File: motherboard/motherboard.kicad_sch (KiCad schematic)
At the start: 57 parts, among them U1 QT1481, U2 cap_touch, U3 cap_touch, k1 cap_touch, k10 cap_touch, k11 cap_touch, k12 cap_touch, k13 cap_touch, k14 cap_touch, k15 cap_touch, k2 cap_touch, k3 cap_touch, k4 cap_touch, k5 cap_touch, k6 cap_touch, k7 cap_touch, k8 cap_touch, k9 cap_touch

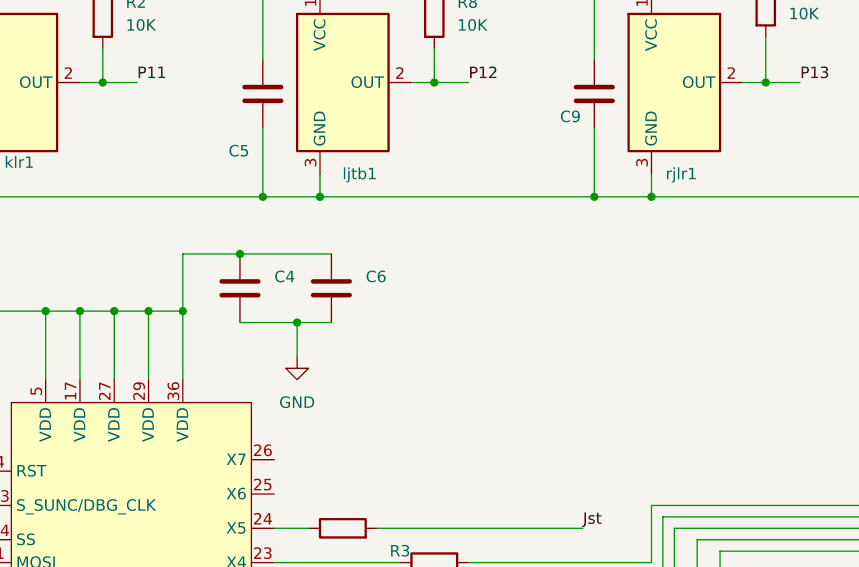
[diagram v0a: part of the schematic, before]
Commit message: fix error hall
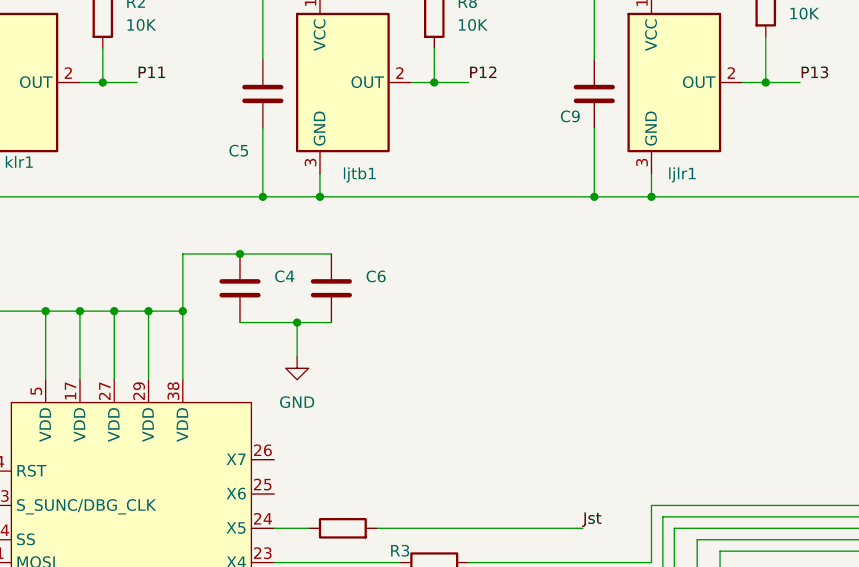
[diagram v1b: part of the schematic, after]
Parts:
- renumbered rjlr1 to ljlr1
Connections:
- net +5V: now also U1.38 (VDD); no longer U1.36 (Y5A)
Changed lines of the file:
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@@
     (pin "34")
     (pin "35")
-    (pin "36")
+    (pin "38")
     (pin "36")
     (pin "37")
@@
   (symbol (lib_id "Sensor_Magnetic:DRV5055A1xDBZxQ1") (at 180.34 44.45 0) (unit 1)
     (in_bom yes) (on_board yes)
-    (property "Reference" "rjlr1" (id 0) (at 182.88 54.61 0)
+    (property "Reference" "ljlr1" (id 0) (at 182.88 54.61 0)
       (effects (font (size 1.27 1.27)) (justify right))
     )
@@
       (reference "ktb1") (unit 1) (value "DRV505") (footprint "Package_TO_SOT_SMD:SOT-23")
     )
+    (path "/a7594aa7-ff91-417c-8749-70aad5ba1e56"
+      (reference "ljlr1") (unit 1) (value "DRV505") (footprint "Package_TO_SOT_SMD:SOT-23")
+    )
     (path "/11d88314-ce06-44e4-976a-1a9db8567436"
       (reference "ljtb1") (unit 1) (value "DRV505") (footprint "Package_TO_SOT_SMD:SOT-23")
     )
-    (path "/a7594aa7-ff91-417c-8749-70aad5ba1e56"
-      (reference "rjlr1") (unit 1) (value "DRV505") (footprint "Package_TO_SOT_SMD:SOT-23")
-    )
     (path "/6bc6018a-8b24-480a-b8c5-125304420071"

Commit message: 3dmother
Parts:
- removed k1, k10, k11, k12, k13, k14, k15, k2, k3, k4, k5, k6, k7, k8, k9: cap_touch, 42QT1481:cap_touch, symbol touch_keys:cap_touch
- added C23, C24, C25, C26, C27, C28, C29, C30, C31, C32, C33, C34, C35, C36, C37, C38, C39, C40, C41, C42, C43, C44, C45, C46, C47, C48, C49, C50, C51, C52, C53, C54, C55, C56: 50pF, Capacitor_Tantalum_SMD:CP_EIA-1608-10_AVX-L_Pad1.25x1.05mm_HandSolder, symbol Device:C
- added U23, U24, U25, U26, U27, U28, U29, U30, U31, U32, U33, U34, U35, U36, U37: cap_touch, 42QT1481:cap_touch, symbol touch_keys:cap_touch
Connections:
- net y3: now reaches R16.2
- net y3: now also C44.2, C46.2, C48.2, C50.2, C52.2
- net at R10.2: now also C31.1, C41.1, C51.1
- net y1: now reaches R13.2
- net y1: now also C24.2, C26.2, C28.2, C30.2, C32.2
- net at R12.2: now also C29.1, C39.1, C49.1
- net x0: now reaches R5.2
- net x0: now also C54.2, C56.2
- net at R4.2: now also C27.1, C37.1, C47.1
- net y2: now reaches R15.2
- net y2: now also C34.2, C36.2, C38.2, C40.2, C42.2
- net at R9.2: now also C25.1, C35.1, C45.1
- net Jst: no longer names the net of R3.2
- net Jst: now also C23.1, C33.1, C43.1
- net jst: no longer names the net of U2.1 (C1)
- net jst: now also C23.2, C24.1; no longer U3.1 (C1)
- new net: C47.2, C48.1, U33.1 (C1)
- new net: C39.2, C40.1, U29.1 (C1)
- new net: C31.2, C32.1, U25.1 (C1)
- new net: C33.2, C34.1, U26.1 (C1)
- new net: C37.2, C38.1, U28.1 (C1)
- new net: C35.2, C36.1, U27.1 (C1)
- new net: C53.2, C54.1, U36.1 (C1)
- new net: C43.2, C44.1, U31.1 (C1)
- new net: C27.2, C28.1, U23.1 (C1)
- new net: C55.1, R18.2
- new net: C55.2, C56.1, U37.1 (C1)
- new net: C41.2, C42.1, U30.1 (C1)
- new net: C45.2, C46.1, U32.1 (C1)
- new net: C51.2, C52.1, U35.1 (C1)
- new net: C29.2, C30.1, U24.1 (C1)
- new net: C49.2, C50.1, U34.1 (C1)
- new net: C25.2, C26.1, U3.1 (C1)
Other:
- moved on the sheet: C10, C11, C3, C4, C6, C7, C8, R10, R11, R12, R13, R14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

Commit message: cp10 to A0
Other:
- sheet Mouse_and_microcontroller ports: added ADC_0, ADC_1; removed GP10, GP11
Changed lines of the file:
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@@
       (effects (font (size 1.27 1.27)) (justify right))
     )
-    (pin "GP10" input (at 54.61 109.22 0)
+    (pin "ADC_0" input (at 54.61 109.22 0)
       (effects (font (size 1.27 1.27)) (justify right))
     )
-    (pin "GP11" input (at 54.61 113.03 0)
+    (pin "ADC_1" input (at 54.61 113.03 0)
       (effects (font (size 1.27 1.27)) (justify right))
     )

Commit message: oh49e
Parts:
- removed R1, R2: 10K, Resistor_SMD:R_0805_2012Metric_Pad1.20x1.40mm_HandSolder, symbol Device:R
- klr1, ktb1: value DRV505 -> (none)
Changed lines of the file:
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@@
   (junction (at 140.97 57.15) (diameter 0) (color 0 0 0 0)
   )
-  (junction (at 116.84 44.45) (diameter 0) (color 0 0 0 0)
-  )
   (junction (at 222.25 119.38) (diameter 0) (color 0 0 0 0)
   )
@@
   (junction (at 96.52 69.85) (diameter 0) (color 0 0 0 0)
   )
-  (junction (at 81.28 44.45) (diameter 0) (color 0 0 0 0)
-  )
   (junction (at 193.04 106.68) (diameter 0) (color 0 0 0 0)
   )
@@
     (stroke (width 0) (type default))
   )
-  (wire (pts (xy 114.3 44.45) (xy 116.84 44.45))
+  (wire (pts (xy 114.3 44.45) (xy 120.65 44.45))
     (stroke (width 0) (type default))
   )
@@
     (stroke (width 0) (type default))
   )
-  (wire (pts (xy 116.84 40.64) (xy 116.84 44.45))
-    (stroke (width 0) (type default))
-  )
   (wire (pts (xy 147.32 101.6) (xy 147.32 67.31))
     (stroke (width 0) (type default))
@@
     (stroke (width 0) (type default))
   )
-  (wire (pts (xy 116.84 25.4) (xy 116.84 33.02))
-    (stroke (width 0) (type default))
-  )
   (wire (pts (xy 95.25 165.1) (xy 95.25 171.45))
     (stroke (width 0) (type default))
@@
     (stroke (width 0) (type default))
   )
-  (wire (pts (xy 81.28 33.02) (xy 81.28 26.67))
-    (stroke (width 0) (type default))
-  )
   (wire (pts (xy 259.08 95.25) (xy 259.08 96.52))
     (stroke (width 0) (type default))
@@
     (stroke (width 0) (type default))
   )
-  (wire (pts (xy 116.84 44.45) (xy 120.65 44.45))
-    (stroke (width 0) (type default))
-  )
   (wire (pts (xy 226.06 39.37) (xy 226.06 44.45))
     (stroke (width 0) (type default))
@@
     (stroke (width 0) (type default))
   )
-  (wire (pts (xy 81.28 40.64) (xy 81.28 44.45))
-    (stroke (width 0) (type default))
-  )
   (wire (pts (xy 204.47 128.27) (xy 204.47 130.81))
     (stroke (width 0) (type default))
@@
     (stroke (width 0) (type default))
   )
-  (wire (pts (xy 78.74 44.45) (xy 81.28 44.45))
+  (wire (pts (xy 78.74 44.45) (xy 83.82 44.45))
     (stroke (width 0) (type default))
   )
@@
     (stroke (width 0) (type default))
   )
-  (wire (pts (xy 81.28 44.45) (xy 83.82 44.45))
-    (stroke (width 0) (type default))
-  )
   (wire (pts (xy 166.37 109.22) (xy 166.37 64.77))
     (stroke (width 0) (type default))
@@
     (effects (font (size 1.27 1.27)) (justify left bottom))
   )
-  (label "+3.3V" (at 116.84 25.4 0) (fields_autoplaced)
-    (effects (font (size 1.27 1.27)) (justify left bottom))
-  )
   (label "P15" (at 266.7 44.45 0) (fields_autoplaced)
     (effects (font (size 1.27 1.27)) (justify left bottom))
@@
     (effects (font (size 1.27 1.27)) (justify left bottom))
   )
-  (label "+3.3V" (at 81.28 26.67 0) (fields_autoplaced)
-    (effects (font (size 1.27 1.27)) (justify left bottom))
-  )
   (label "P10" (at 83.82 44.45 0) (fields_autoplaced)
     (effects (font (size 1.27 1.27)) (justify left bottom))
@@
       (effects (font (size 1.27 1.27)) (justify right))
     )
-    (property "Value" "DRV505" (at 100.33 45.7199 0)
+    (property "Value" "" (at 100.33 45.7199 0)
       (effects (font (size 1.27 1.27)) (justify right) hide)
     )
@@
       (effects (font (size 1.27 1.27)) hide)
     )
-    (property "Datasheet" "https://www.ti.com/lit/ds/symlink/drv5055-q1.pdf" (at 106.68 44.45 0)
+    (property "Datasheet" "https://www.progrexa.com/file_PDF/OH49E.pdf" (at 106.68 44.45 0)
       (effects (font (size 1.27 1.27)) hide)
     )
@@
       (effects (font (size 1.27 1.27)) (justify right))
     )
-    (property "Value" "DRV505" (at 64.77 45.7199 0)
+    (property "Value" "" (at 64.77 45.7199 0)
       (effects (font (size 1.27 1.27)) (justify right) hide)
     )
@@
       (effects (font (size 1.27 1.27)) hide)
     )
-    (property "Datasheet" "https://www.ti.com/lit/ds/symlink/drv5055-q1.pdf" (at 71.12 44.45 0)
+    (property "Datasheet" "https://www.progrexa.com/file_PDF/OH49E.pdf" (at 71.12 44.45 0)
       (effects (font (size 1.27 1.27)) hide)
     )
@@
     )
   )
-  (symbol (lib_id "Device:R") (at 116.84 36.83 0) (unit 1)
-    (in_bom yes) (on_board yes) (dnp no) (fields_autoplaced)
-    (property "Reference" "R2" (at 119.38 35.5599 0)
-      (effects (font (size 1.27 1.27)) (justify left))
-    )
-    (property "Value" "10K" (at 119.38 38.0999 0)
-      (effects (font (size 1.27 1.27)) (justify left))
-    )
-    (property "Footprint" "Resistor_SMD:R_0805_2012Metric_Pad1.20x1.40mm_HandSolder" (at 115.062 36.83 90)
-      (effects (font (size 1.27 1.27)) hide)
-    )
-    (property "Datasheet" "~" (at 116.84 36.83 0)
-      (effects (font (size 1.27 1.27)) hide)
-    )
-    (pin "1")
-    (pin "2")
-    (instances
-      (project "motherboard"
-        (path "/99157713-5a67-456e-be9f-48b28b564fb7"
-          (reference "R2") (unit 1)
-        )
-      )
-    )
-  )
   (symbol (lib_id "touch_keys:cap_touch") (at 204.47 85.09 0) (unit 1)
     (in_bom yes) (on_board yes) (dnp no)
@@
         )
       )
-    )
-  )
-  (symbol (lib_id "Device:R") (at 81.28 36.83 0) (unit 1)
-    (in_bom yes) (on_board yes) (dnp no) (fields_autoplaced)
-    (property "Reference" "R1" (at 83.82 35.5599 0)
-      (effects (font (size 1.27 1.27)) (justify left))
-    )
-    (property "Value" "10K" (at 83.82 38.0999 0)
-      (effects (font (size 1.27 1.27)) (justify left))
-    )
-    (property "Footprint" "Resistor_SMD:R_0805_2012Metric_Pad1.20x1.40mm_HandSolder" (at 79.502 36.83 90)
-      (effects (font (size 1.27 1.27)) hide)
-    )
-    (property "Datasheet" "~" (at 81.28 36.83 0)
-      (effects (font (size 1.27 1.27)) hide)
-    )
-    (pin "1")
-    (pin "2")
-    (instances
-      (project "motherboard"
-        (path "/99157713-5a67-456e-be9f-48b28b564fb7"
-          (reference "R1") (unit 1)
-        )
-      )

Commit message: mpr121
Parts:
- removed C10, C11, C7, C8: 4.7nF, Capacitor_Tantalum_SMD:CP_EIA-2012-15_AVX-P_Pad1.30x1.05mm_HandSolder, symbol Device:C
- removed C3: 4.7uF, Capacitor_Tantalum_SMD:CP_EIA-6032-15_Kemet-U_Pad2.25x2.35mm_HandSolder, symbol Device:C
- removed C4, C6: 0.1uF, Capacitor_Tantalum_SMD:CP_EIA-3528-12_Kemet-T_Pad1.50x2.35mm_HandSolder, symbol Device:C
- removed C53, C55: 50pF, Capacitor_Tantalum_SMD:CP_EIA-1608-10_AVX-L_Pad1.25x1.05mm_HandSolder, symbol Device:C
- removed R10, R12, R13, R15, R16, R18, R3, R4, R5, R9: 1K, Resistor_SMD:R_1206_3216Metric_Pad1.30x1.75mm_HandSolder, symbol Device:R
- removed R11, R14, R6, R7: 470K, Resistor_SMD:R_0805_2012Metric_Pad1.20x1.40mm_HandSolder, symbol Device:R
- removed R17, R19, R20, R8: 10K, Resistor_SMD:R_0805_2012Metric_Pad1.20x1.40mm_HandSolder, symbol Device:R
- removed U1: QT1481, 42QT1481:QT1481, symbol touch_keys:QT1481
- added U1: MPR121QR2, Package_DFN_QFN:UQFN-20_3x3mm_P0.4mm, symbol Sensor_Touch:MPR121QR2
- klr1, ktb1: value (none) -> ~
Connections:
- net GND: now also U1.6 (VSS)
- net y1: now also U1.8 (ELE0)
- net y2: now also U1.9 (ELE1)
- net y3: now also U1.10 (ELE2)
- net x5: now reaches C31.1, C41.1, C51.1
- net x5: now also U1.15 (LED3/ELE7)
- net x1: now reaches C23.1, C33.1, C43.1
- net x1: now also U1.11 (ELE3)
- net x3: now reaches C27.1, C37.1, C47.1
- net x3: now also U1.13 (LED1/ELE5)
- net x2: now reaches C25.1, C35.1, C45.1
- net x2: now also U1.12 (LED0/ELE4)
- net x4: now reaches C29.1, C39.1, C49.1
- net x4: now also U1.14 (LED2/ELE6)
- net x0 renamed Lx
- net Lx: now also U1.16 (LED4/ELE8); no longer C56.2
- new net 3V3: U1.20 (VDD)
- new net Mouse_and_microcontroller/GP4: U1.3 (SDA)
- new net Mouse_and_microcontroller/GP5: U1.2 (SCL)
- new net Rx: C56.2, U1.17 (LED5/ELE9)
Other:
- sheet Mouse_and_microcontroller ports: added GP4, GP5; removed GP16, GP17, GP18, GP19

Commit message: diodes
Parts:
- removed C23, C24, C25, C26, C27, C28, C29, C30, C31, C32, C33, C34, C35, C36, C37, C38, C39, C40, C41, C42, C43, C44, C45, C46, C47, C48, C49, C50, C51, C52, C54, C56: 50pF, Capacitor_Tantalum_SMD:CP_EIA-1608-10_AVX-L_Pad1.25x1.05mm_HandSolder, symbol Device:C
- added D1, D10, D11, D12, D13, D14, D15, D16, D17, D18, D19, D2, D20, D21, D22, D23, D24, D25, D26, D27, D28, D29, D30, D31, D4, D5, D6, D7, D8, D9: 1N4148WT, Diode_SMD:D_SOD-523, symbol Diode:1N4148WT
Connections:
- net Lx: now also U36.1 (C1)
- net Rx: now also U37.1 (C1)
- net x1: now also D1.2 (A), D12.2 (A), D22.2 (A)
- net x2: now also D14.2 (A), D24.2 (A), D4.2 (A)
- net x3: now also D16.2 (A), D26.2 (A), D6.2 (A)
- net x4: now also D18.2 (A), D28.2 (A), D8.2 (A)
- net x5: now also D10.2 (A), D20.2 (A), D30.2 (A)
- net y1: now also D11.2 (A), D2.2 (A), D5.2 (A), D7.2 (A), D9.2 (A)
- net y2: now also D13.2 (A), D15.2 (A), D17.2 (A), D19.2 (A), D21.2 (A)
- net y3: now also D23.2 (A), D25.2 (A), D27.2 (A), D29.2 (A), D31.2 (A)
- net at U33.1 (C1): now also D26.1 (K), D27.1 (K)
- net at U29.1 (C1): now also D18.1 (K), D19.1 (K)
- net at U25.1 (C1): now also D10.1 (K), D11.1 (K)
- net at U26.1 (C1): now also D12.1 (K), D13.1 (K)
- net at U28.1 (C1): now also D16.1 (K), D17.1 (K)
- net at U2.1 (C1): now also D1.1 (K), D2.1 (K)
- net at U27.1 (C1): now also D14.1 (K), D15.1 (K)
- net at U31.1 (C1): now also D22.1 (K), D23.1 (K)
- net at U23.1 (C1): now also D6.1 (K), D7.1 (K)
- net at U30.1 (C1): now also D20.1 (K), D21.1 (K)
- net at U32.1 (C1): now also D24.1 (K), D25.1 (K)
- net at U35.1 (C1): now also D30.1 (K), D31.1 (K)
- net at U24.1 (C1): now also D8.1 (K), D9.1 (K)
- net at U34.1 (C1): now also D28.1 (K), D29.1 (K)
- net at U3.1 (C1): now also D4.1 (K), D5.1 (K)
